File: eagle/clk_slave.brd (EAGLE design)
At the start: 31.8 x 16.5 mm, 47 parts

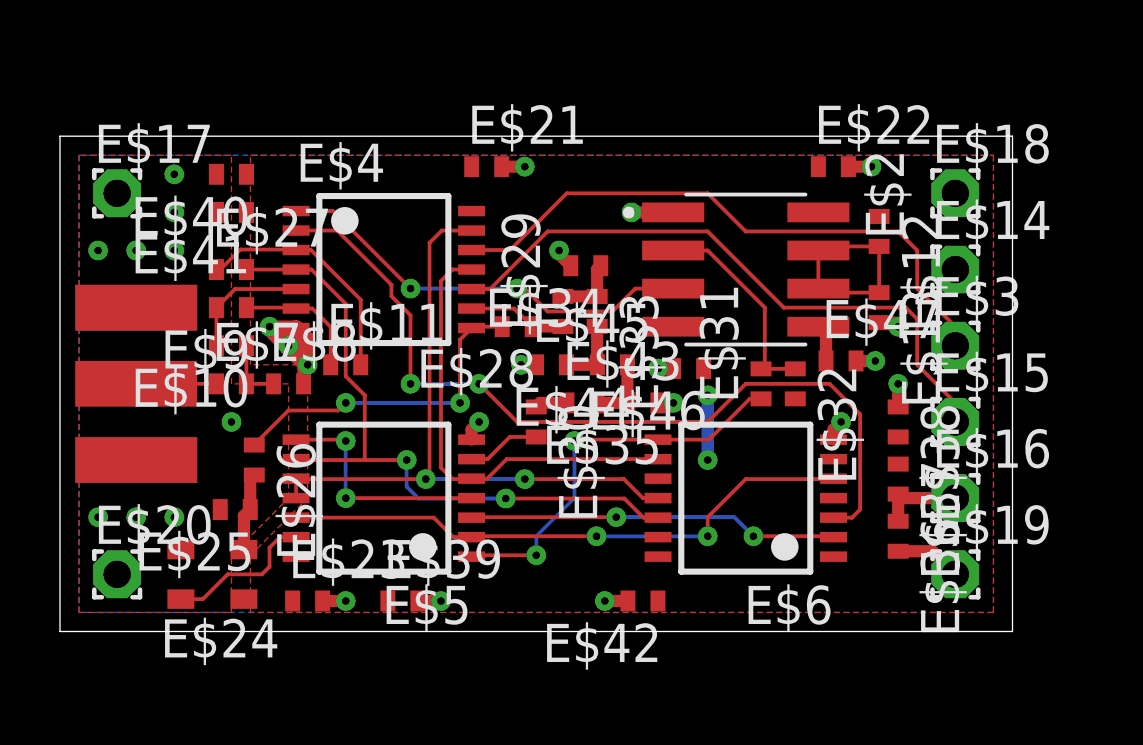
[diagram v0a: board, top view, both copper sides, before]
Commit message: clean up slave clock board layout
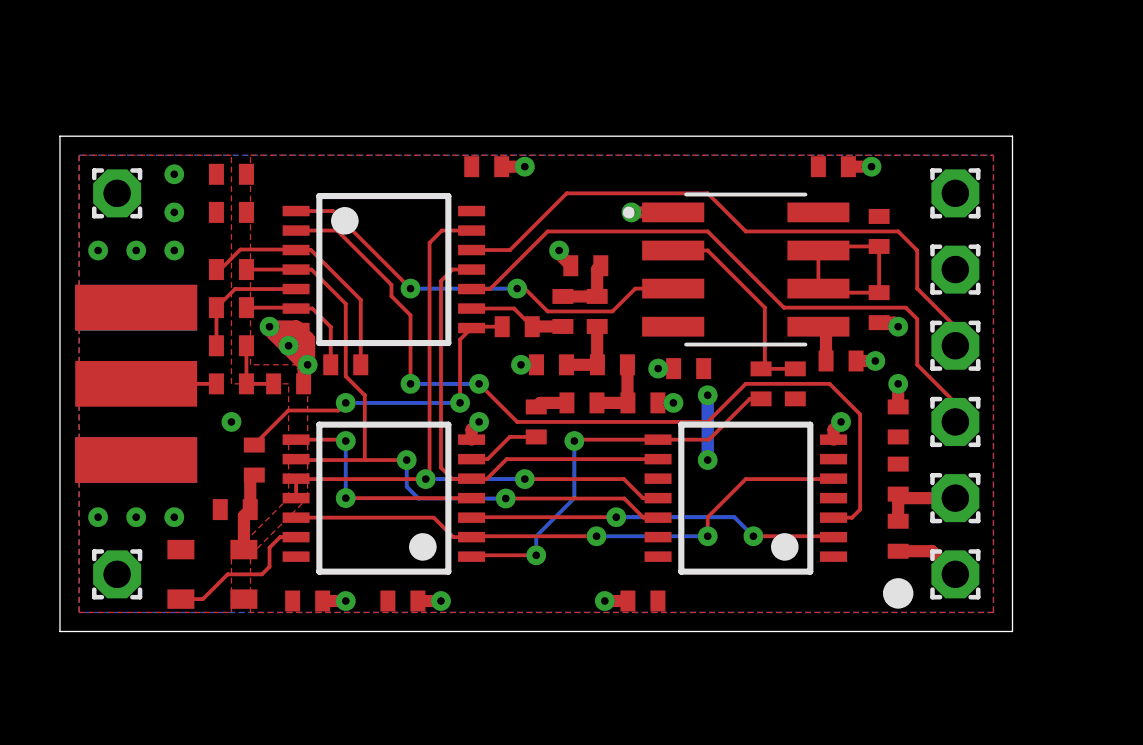
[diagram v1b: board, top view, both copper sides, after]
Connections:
- net S$1 renamed CLK
- net S$13 renamed BPSK
- net S$14 renamed INV
- net S$15 renamed DPPS
- net S$16 renamed PERR
- net S$18 renamed DINV
- net S$19 renamed TRIG
- net S$2 renamed PPS
- net S$20 renamed !DPPS
- net S$21 renamed SPPS
- net S$22 renamed !SPPS
- net S$25 renamed FB
- net S$27 renamed VIN
- net S$3 renamed RC
- net S$30 renamed CV
- net S$4 renamed OSC
- net S$5 renamed OCLK
- net S$6 renamed VFB
- net S$7 renamed FILT
- net S$8 renamed CLK_IN

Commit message: update slave clock design
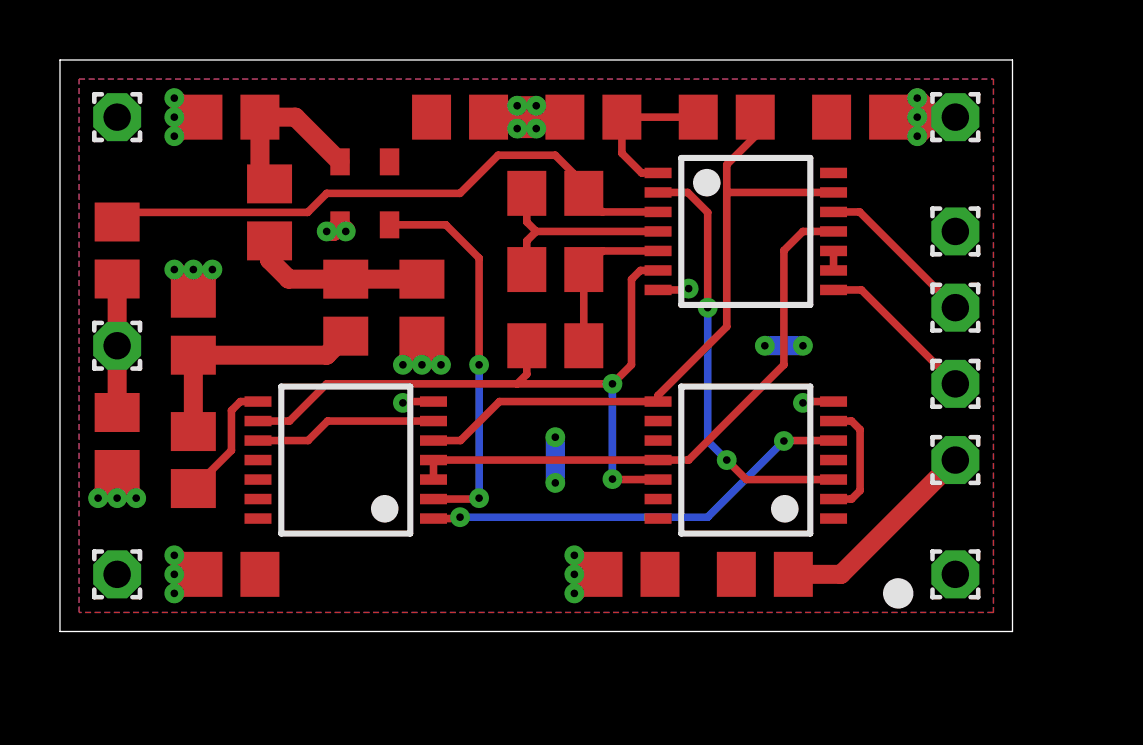
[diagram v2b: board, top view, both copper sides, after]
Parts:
- removed E$1: (no value), SparkFun-Retired:SMA-EDGE
- removed E$10, E$11, E$12, E$13, E$21, E$22, E$23, E$25, E$26, E$27, E$28, E$29, E$30, E$31, E$32, E$33, E$34, E$35, E$36, E$37, E$38, E$39, E$40, E$41, E$42, E$43, E$44, E$45, E$46, E$47, E$7, E$8, E$9: (no value), BeagleBone_Black_Wireless:R0402
- removed E$14, E$15, E$16, E$17, E$18, E$3: (no value), wirepad:1,6/0,9
- removed E$2: (no value), IC:8-SOIC
- removed E$24: (no value), crystal:ASE
- removed E$4, E$5, E$6: (no value), 74xx-us:TSSOP14
- added C1, C10: 1n, ref-packages:R0805
- added C2: 470n, ref-packages:R0805
- added C3: 220n, ref-packages:R0805
- added C4, C5, C6, C7, C8: 100n, ref-packages:R0805
- added C9: 10u, ref-packages:R0805
- added L1: FERRITE, ref-packages:R0805
- added P1, P2, P5, P6, P7, P8, P9: (no value), wirepad:1,6/0,9
- added R1, R4: 49.9, ref-packages:R0805
- added R2: 220, ref-packages:R0805
- added R3: 100, ref-packages:R0805
- added R5: 47k, ref-packages:R0805
- added R6, R7: 33k, ref-packages:R0805
- added U1: SIT3808AI-22-33NB-25.000000Y, crystal:ASE
- added U2: 74LVCU04A, 74xx-us:TSSOP14
- added U3: 74LVC86A, 74xx-us:TSSOP14
- added U4: 74LVC74A, 74xx-us:TSSOP14
- renumbered E$19 to P4, E$20 to P3
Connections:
- removed net !DPPS: E$31.1, E$5.1, E$6.8
- removed net !SPPS: E$2.3, E$4.1
- removed net CLK_IN: E$1.SIG, E$7.1
- removed net CV: E$2.5, E$47.1
- removed net DINV: E$5.3, E$6.2
- removed net DPPS: E$4.11, E$5.5, E$6.9
- removed net FB: E$30.2, E$5.6
- removed net FILT: E$26.1, E$28.2, E$4.8
- removed net PERR: E$5.4, E$5.8
- removed net RC: E$12.2, E$13.1, E$2.6, E$2.7
- removed net S$10: E$10.2, E$4.5, E$9.2
- removed net S$11: E$11.1, E$4.6, E$9.1
- removed net S$12: E$11.2, E$27.1, E$4.3
- removed net S$17: E$28.1, E$29.1, E$4.9
- removed net S$23: E$29.2, E$33.1, E$34.1
- removed net S$26: E$30.1, E$43.1
- removed net S$28: E$35.2, E$43.2, E$44.1
- removed net S$29: E$33.2, E$44.2, E$45.2
- removed net S$9: E$10.1, E$7.2, E$8.1
- removed net SPPS: E$4.2, E$6.3
- removed net TRIG: E$2.2, E$31.2, E$32.1
- new net !INV: U4.2, U4.6
- new net !OCLK: U2.10, U2.9
- new net !PPS: R5.1, U2.13, U3.5, U4.8
- new net ALIGN: R4.1, U3.8
- new net AMP1: C1.2, R6.1, U2.3
- new net AMP2: C10.1, R6.2, U2.4
- new net AMP3: C10.2, R7.1, U2.5
- new net DELAY: C9.2, R5.2, U2.1
- new net FILT1: C4.2, R3.2, R4.2
- new net FILT2: C3.1, R2.2, R3.1
- new net LCLK: U3.10, U3.6
- new net SRC: C1.1, P2.1, R1.1
- new net TOGGLE: U2.2, U4.3
- net BPSK: now also R7.2, U2.6, U3.9, U4.12; no longer E$27.2, E$4.4, E$5.9, E$6.12
- net CLK: now also P6.1, U2.8; no longer E$3.1, E$4.12
- net GND: now also C2.2, C3.2, C4.1, C5.2, C6.2, C7.2, C8.2, C9.1, P1.1, P8.1, P9.1, R1.2, U1.2, U2.7, U3.7, U4.7; no longer E$1.GND@0, E$1.GND@1, E$1.GND@2, E$1.GND@3, E$13.2, E$14.1, E$17.1, E$18.1, E$2.1, E$21.2, E$22.2, E$23.2, E$24.2, E$25.2, E$34.2, E$35.1, E$36.2, E$38.1, E$39.2, E$4.7, E$40.2, E$41.2, E$42.2, E$45.1, E$46.2, E$47.2, E$5.7, E$6.7, E$8.2
- net INV: now also U3.1, U4.5; no longer E$5.12, E$5.2, E$6.5
- net OCLK: now also U2.11, U3.3, U3.4, U4.11; no longer E$4.13, E$5.10, E$5.11, E$6.11
- net OSC: now also U1.3, U3.2; no longer E$24.3, E$5.13
- net PPS: now also P7.1, U2.12; no longer E$15.1, E$4.10
- net V3.3: now also C5.1, C6.1, C7.1, C8.1, L1.2, U1.4, U2.14, U3.12, U3.13, U3.14, U4.1, U4.10, U4.13, U4.14, U4.4; no longer E$12.1, E$2.4, E$2.8, E$21.1, E$22.1, E$23.1, E$24.4, E$32.2, E$37.1, E$38.2, E$39.1, E$4.14, E$40.1, E$41.1, E$42.1, E$46.1, E$5.14, E$6.1, E$6.10, E$6.13, E$6.14, E$6.4
- net VFB: now also C2.1, R2.1, U1.1; no longer E$24.1, E$25.1, E$26.2
- net VIN: now also L1.1, P5.1; no longer E$16.1, E$36.1, E$37.2
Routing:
- net SPPS: track 28.1 -> 0.00 mm, vias 2 -> 0
- net !PPS: track 0.00 -> 22.4 mm
- net AMP1: track 0.00 -> 19.9 mm
- net GND: track 18.6 -> 35.6 mm, vias 27 -> 30
- net PPS: track 20.8 -> 5.38 mm
- net DPPS: track 15.1 -> 0.00 mm
- net CLK: track 20.1 -> 5.36 mm
- net TOGGLE: track 0.00 -> 14.3 mm, vias 0 -> 2
- net !SPPS: track 14.3 -> 0.00 mm, vias 2 -> 0
- net !DPPS: track 13.3 -> 0.00 mm, vias 2 -> 0
- net DINV: track 12.3 -> 0.00 mm, vias 2 -> 0
- net FILT: track 11.1 -> 0.00 mm, vias 2 -> 0
- net S$12: track 7.95 -> 0.00 mm
- net OSC: track 5.07 -> 13.0 mm, vias 0 -> 2
- net FILT1: track 0.00 -> 7.89 mm
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- removed copper zone on layer 1, net GND
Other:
- board size 31.8 x 16.5 mm -> 31.8 x 19.1 mm

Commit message: reduce slave clock drift to <1Hz RMS
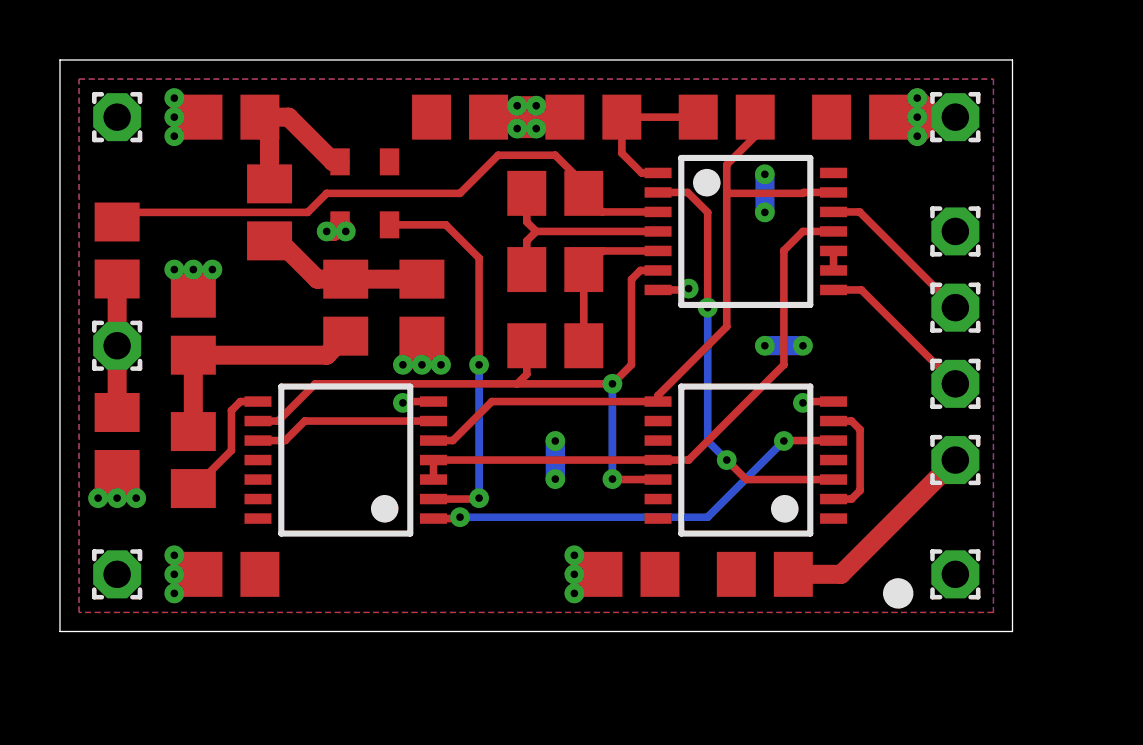
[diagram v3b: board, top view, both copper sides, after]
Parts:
- C2: value 470n -> 1u
- C3: value 220n -> 330n
- R4: value 49.9 -> 47
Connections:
- net VFB renamed FB
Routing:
- net V3.3: track 2.79 -> 3.81 mm, vias 4 -> 6
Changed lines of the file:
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@@
 <element name="C1" library="ref-packages" library_urn="urn:adsk.eagle:library:338" package="R0805" value="1n" x="1.905" y="12.7" smashed="yes" rot="R90"/>
 <element name="R2" library="ref-packages" library_urn="urn:adsk.eagle:library:338" package="R0805" value="220" x="6.985" y="13.97" smashed="yes" rot="R270"/>
-<element name="C2" library="ref-packages" library_urn="urn:adsk.eagle:library:338" package="R0805" value="470n" x="5.715" y="17.145" smashed="yes" rot="R180"/>
-<element name="C3" library="ref-packages" library_urn="urn:adsk.eagle:library:338" package="R0805" value="220n" x="12.065" y="10.795" smashed="yes" rot="R270"/>
+<element name="C2" library="ref-packages" library_urn="urn:adsk.eagle:library:338" package="R0805" value="1u" x="5.715" y="17.145" smashed="yes" rot="R180"/>
+<element name="C3" library="ref-packages" library_urn="urn:adsk.eagle:library:338" package="R0805" value="330n" x="12.065" y="10.795" smashed="yes" rot="R270"/>
 <element name="R3" library="ref-packages" library_urn="urn:adsk.eagle:library:338" package="R0805" value="100" x="9.525" y="10.795" smashed="yes" rot="R270"/>
 <element name="C4" library="ref-packages" library_urn="urn:adsk.eagle:library:338" package="R0805" value="100n" x="4.445" y="10.16" smashed="yes" rot="R270"/>
-<element name="R4" library="ref-packages" library_urn="urn:adsk.eagle:library:338" package="R0805" value="49.9" x="4.445" y="5.715" smashed="yes" rot="R90"/>
+<element name="R4" library="ref-packages" library_urn="urn:adsk.eagle:library:338" package="R0805" value="47" x="4.445" y="5.715" smashed="yes" rot="R90"/>
 <element name="C5" library="ref-packages" library_urn="urn:adsk.eagle:library:338" package="R0805" value="100n" x="5.715" y="1.905" smashed="yes" rot="R180"/>
 <element name="C6" library="ref-packages" library_urn="urn:adsk.eagle:library:338" package="R0805" value="100n" x="13.335" y="17.145" smashed="yes"/>
@@
 <contactref element="U3" pad="13"/>
 <contactref element="U3" pad="12"/>
-<via x="16.51" y="6.477" extent="1-16" drill="0.254"/>
-<via x="16.51" y="4.953" extent="1-16" drill="0.254"/>
-<wire x1="16.51" y1="6.477" x2="16.51" y2="4.953" width="0.635" layer="16"/>
+<via x="16.51" y="6.35" extent="1-16" drill="0.254"/>
+<via x="16.51" y="5.08" extent="1-16" drill="0.254"/>
+<wire x1="16.51" y1="6.35" x2="16.51" y2="5.08" width="0.635" layer="16"/>
 <contactref element="L1" pad="2"/>
 <via x="23.495" y="9.525" extent="1-16" drill="0.254"/>
 <via x="24.765" y="9.525" extent="1-16" drill="0.254"/>
 <wire x1="23.495" y1="9.525" x2="24.765" y2="9.525" width="0.635" layer="16"/>
-</signal>
-<signal name="VFB">
+<via x="23.495" y="15.24" extent="1-16" drill="0.254"/>
+<via x="23.495" y="13.97" extent="1-16" drill="0.254"/>
+<wire x1="23.495" y1="15.24" x2="23.495" y2="13.97" width="0.635" layer="16"/>
+</signal>
+<signal name="FB">
 <contactref element="U1" pad="1"/>
 <contactref element="C2" pad="1"/>
 <contactref element="R2" pad="1"/>
-<wire x1="6.985" y1="14.92" x2="6.665" y2="15.24" width="0.635" layer="1"/>
-<wire x1="6.665" y1="17.145" x2="6.665" y2="15.24" width="0.635" layer="1"/>
-<wire x1="9.335" y1="15.655" x2="7.845" y2="17.145" width="0.635" layer="1"/>
-<wire x1="7.845" y1="17.145" x2="6.665" y2="17.145" width="0.635" layer="1"/>
+<wire x1="6.665" y1="17.145" x2="6.665" y2="16.83" width="0.635" layer="1"/>
+<wire x1="6.665" y1="16.83" x2="6.985" y2="16.51" width="0.635" layer="1"/>
+<wire x1="6.985" y1="16.51" x2="6.985" y2="14.92" width="0.635" layer="1"/>
+<wire x1="9.335" y1="15.655" x2="9.11" y2="15.655" width="0.635" layer="1"/>
+<wire x1="7.62" y1="17.145" x2="6.665" y2="17.145" width="0.635" layer="1"/>
+<wire x1="9.11" y1="15.655" x2="7.62" y2="17.145" width="0.635" layer="1"/>
 </signal>
 <signal name="BPSK">
@@
 <wire x1="15.56" y1="8.575" x2="15.24" y2="8.255" width="0.254" layer="1"/>
 <contactref element="U3" pad="9"/>
-<wire x1="6.6" y1="7.015" x2="7.65" y2="7.015" width="0.254" layer="1"/>
-<wire x1="7.65" y1="7.015" x2="8.89" y2="8.255" width="0.254" layer="1"/>
-<wire x1="8.89" y1="8.255" x2="15.24" y2="8.255" width="0.254" layer="1"/>
+<wire x1="6.6" y1="7.015" x2="7.269" y2="7.015" width="0.254" layer="1"/>
+<wire x1="7.269" y1="7.015" x2="8.509" y2="8.255" width="0.254" layer="1"/>
+<wire x1="8.509" y1="8.255" x2="15.24" y2="8.255" width="0.254" layer="1"/>
 <contactref element="U4" pad="12"/>
 <via x="18.415" y="8.255" extent="1-16" drill="0.254"/>
@@
 <contactref element="R2" pad="2"/>
 <wire x1="12.065" y1="11.745" x2="9.525" y2="11.745" width="0.635" layer="1"/>
-<wire x1="9.525" y1="11.745" x2="7.62" y2="11.745" width="0.635" layer="1"/>
-<wire x1="7.62" y1="11.75" x2="7.62" y2="11.745" width="0.254" layer="1"/>
-<wire x1="7.62" y1="11.75" x2="6.985" y2="12.385" width="0.635" layer="1"/>
-<wire x1="6.985" y1="12.385" x2="6.985" y2="13.02" width="0.635" layer="1"/>
+<wire x1="6.985" y1="13.02" x2="7.3" y2="13.02" width="0.635" layer="1"/>
+<wire x1="8.575" y1="11.745" x2="9.525" y2="11.745" width="0.635" layer="1"/>
+<wire x1="7.3" y1="13.02" x2="8.575" y2="11.745" width="0.635" layer="1"/>
 </signal>
 <signal name="PPS">
@@
 <contactref element="U2" pad="13"/>
 <contactref element="R5" pad="1"/>
-<wire x1="13.35" y1="6.365" x2="12.45" y2="6.365" width="0.254" layer="1"/>
-<wire x1="19.935" y1="7.665" x2="14.65" y2="7.665" width="0.254" layer="1"/>
-<wire x1="14.65" y1="7.665" x2="13.35" y2="6.365" width="0.254" layer="1"/>
+<wire x1="13.096" y1="6.365" x2="12.45" y2="6.365" width="0.254" layer="1"/>
+<wire x1="19.935" y1="7.665" x2="14.396" y2="7.665" width="0.254" layer="1"/>
+<wire x1="14.396" y1="7.665" x2="13.096" y2="6.365" width="0.254" layer="1"/>
 <wire x1="19.935" y1="7.665" x2="19.935" y2="7.87" width="0.254" layer="1"/>
 <wire x1="22.225" y1="10.16" x2="19.935" y2="7.87" width="0.254" layer="1"/>
@@
 <wire x1="22.225" y1="10.16" x2="22.225" y2="14.605" width="0.254" layer="1"/>
 <wire x1="22.225" y1="14.605" x2="22.225" y2="15.56" width="0.254" layer="1"/>
-<wire x1="25.785" y1="14.635" x2="22.255" y2="14.635" width="0.254" layer="1"/>
-<wire x1="22.255" y1="14.635" x2="22.225" y2="14.605" width="0.254" layer="1"/>
+<wire x1="24.765" y1="14.605" x2="22.225" y2="14.605" width="0.254" layer="1"/>
+<wire x1="25.785" y1="14.635" x2="24.795" y2="14.635" width="0.254" layer="1"/>
+<wire x1="24.795" y1="14.635" x2="24.765" y2="14.605" width="0.254" layer="1"/>
 </signal>
 <signal name="AMP2">
@@
 <contactref element="U3" pad="6"/>
 <contactref element="U3" pad="10"/>
-<wire x1="8.27" y1="6.365" x2="6.6" y2="6.365" width="0.254" layer="1"/>
-<wire x1="12.45" y1="7.015" x2="8.92" y2="7.015" width="0.254" layer="1"/>
-<wire x1="8.92" y1="7.015" x2="8.27" y2="6.365" width="0.254" layer="1"/>
+<wire x1="7.508" y1="6.365" x2="6.6" y2="6.365" width="0.254" layer="1"/>
+<wire x1="12.45" y1="7.015" x2="8.158" y2="7.015" width="0.254" layer="1"/>
+<wire x1="8.158" y1="7.015" x2="7.508" y2="6.365" width="0.254" layer="1"/>
 </signal>
 <signal name="OCLK">

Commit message: reduce slave clock drift to <1Hz RMS
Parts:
- R2: value 220 -> 330
- R4: value 47 -> 33
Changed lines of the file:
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@@
 <element name="R1" library="ref-packages" library_urn="urn:adsk.eagle:library:338" package="R0805" value="49.9" x="1.905" y="6.35" smashed="yes" rot="R270"/>
 <element name="C1" library="ref-packages" library_urn="urn:adsk.eagle:library:338" package="R0805" value="1n" x="1.905" y="12.7" smashed="yes" rot="R90"/>
-<element name="R2" library="ref-packages" library_urn="urn:adsk.eagle:library:338" package="R0805" value="220" x="6.985" y="13.97" smashed="yes" rot="R270"/>
+<element name="R2" library="ref-packages" library_urn="urn:adsk.eagle:library:338" package="R0805" value="330" x="6.985" y="13.97" smashed="yes" rot="R270"/>
 <element name="C2" library="ref-packages" library_urn="urn:adsk.eagle:library:338" package="R0805" value="1u" x="5.715" y="17.145" smashed="yes" rot="R180"/>
 <element name="C3" library="ref-packages" library_urn="urn:adsk.eagle:library:338" package="R0805" value="330n" x="12.065" y="10.795" smashed="yes" rot="R270"/>
 <element name="R3" library="ref-packages" library_urn="urn:adsk.eagle:library:338" package="R0805" value="100" x="9.525" y="10.795" smashed="yes" rot="R270"/>
 <element name="C4" library="ref-packages" library_urn="urn:adsk.eagle:library:338" package="R0805" value="100n" x="4.445" y="10.16" smashed="yes" rot="R270"/>
-<element name="R4" library="ref-packages" library_urn="urn:adsk.eagle:library:338" package="R0805" value="47" x="4.445" y="5.715" smashed="yes" rot="R90"/>
+<element name="R4" library="ref-packages" library_urn="urn:adsk.eagle:library:338" package="R0805" value="33" x="4.445" y="5.715" smashed="yes" rot="R90"/>
 <element name="C5" library="ref-packages" library_urn="urn:adsk.eagle:library:338" package="R0805" value="100n" x="5.715" y="1.905" smashed="yes" rot="R180"/>
 <element name="C6" library="ref-packages" library_urn="urn:adsk.eagle:library:338" package="R0805" value="100n" x="13.335" y="17.145" smashed="yes"/>
